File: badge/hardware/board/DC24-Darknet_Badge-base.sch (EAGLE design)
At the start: 54 parts, among them Q1 SOP22, SW0 SWITCH_TACTILETACTILE-2PIN-NA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, SW1 SWITCH_TACTILETACTILE-2PIN-NA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, SW2 SWITCH_TACTILETACTILE-2PIN-NA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, SW3 SWITCH_TACTILETACTILE-2PIN-NA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, SW4 SWITCH_TACTILETACTILE-2PIN-NA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, SW5 SWITCH_TACTILETACTILE-2PIN-NA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, SW6 SWITCH_TACTILETACTILE-2PIN-NA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, SW7 SWITCH_TACTILETACTILE-2PIN-NA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, SW8 SWITCH_TACTILETACTILE-2PIN-NA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

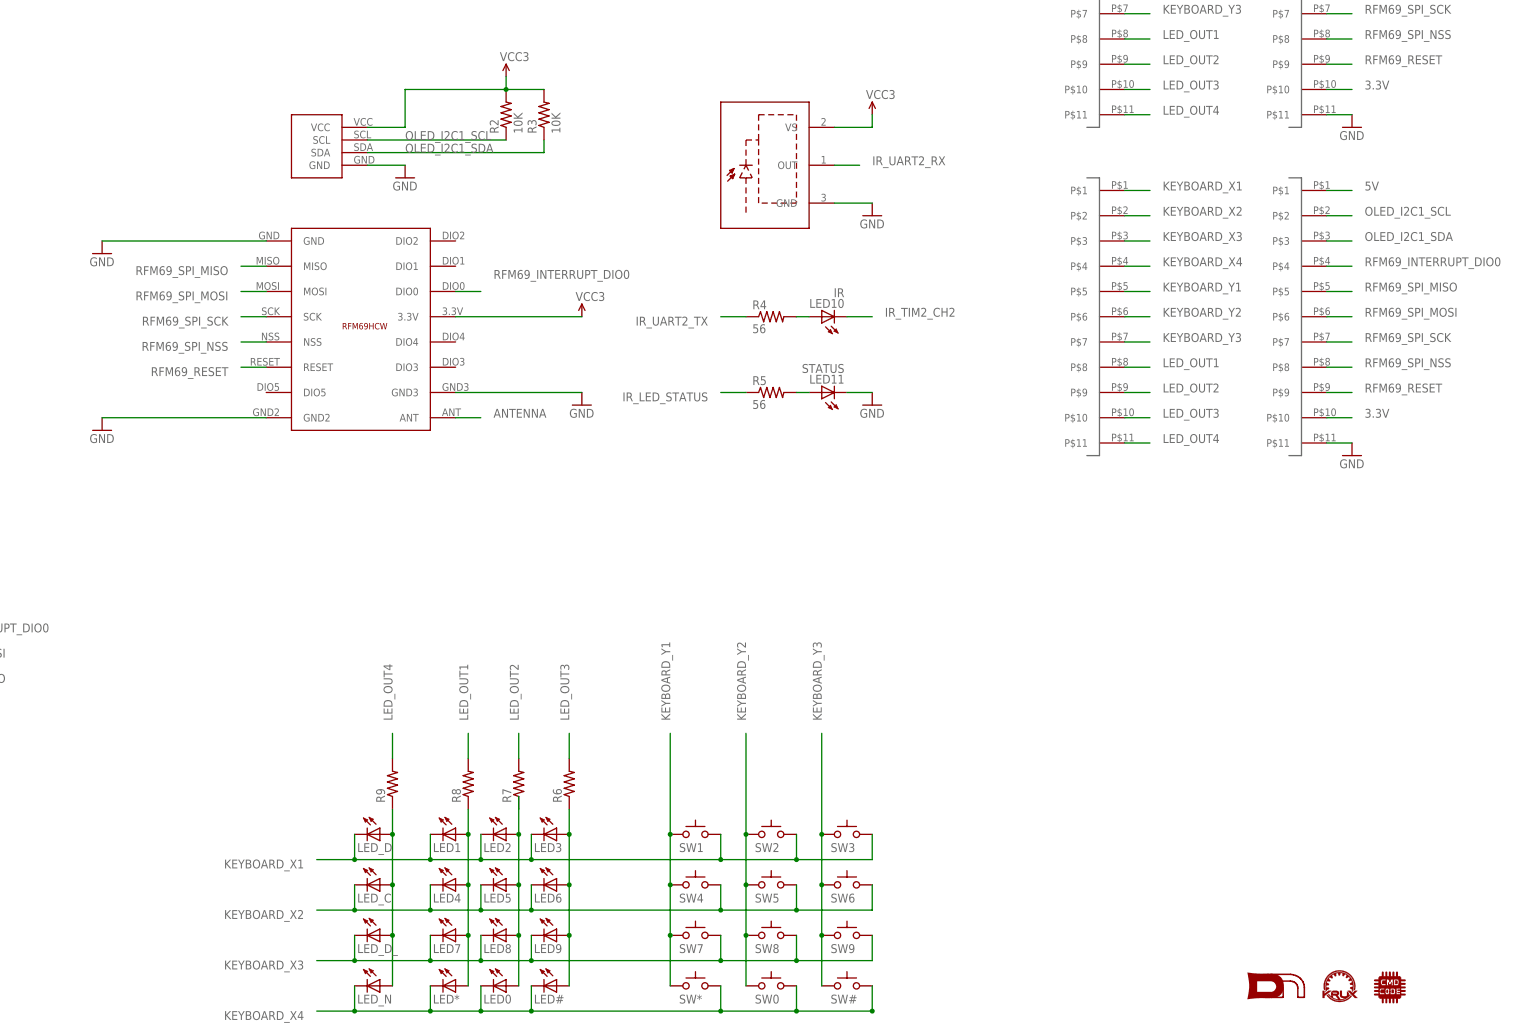
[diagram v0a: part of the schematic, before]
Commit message: moved board files over so we don't lose them
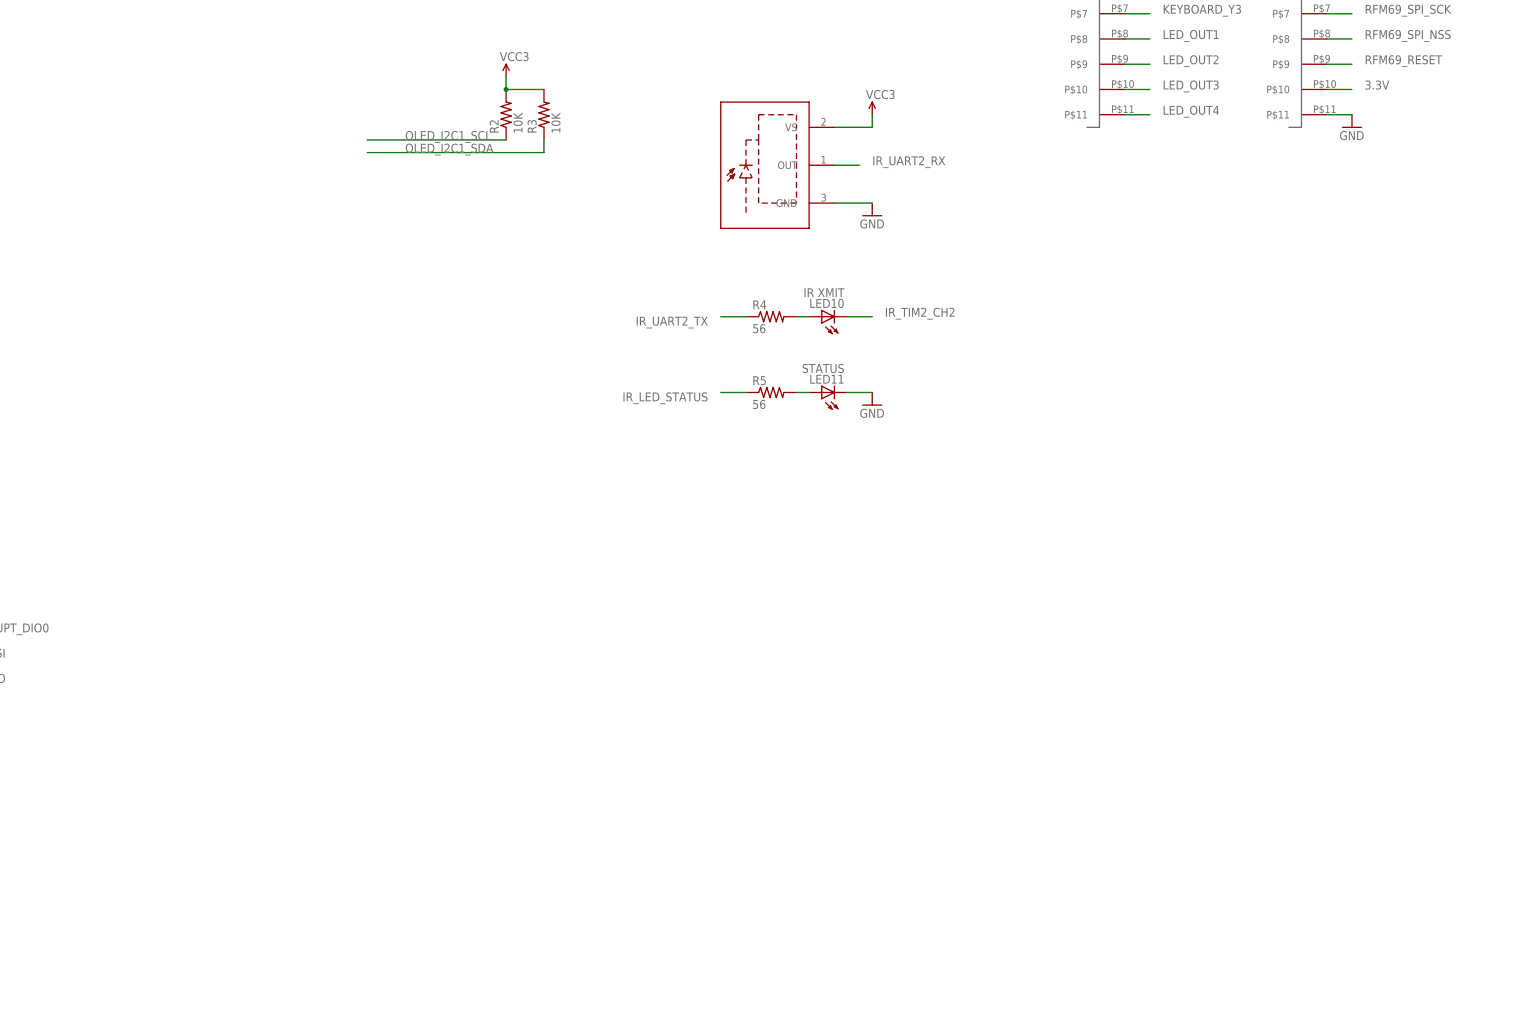
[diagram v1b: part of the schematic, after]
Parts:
- removed LED#, LED*, LED0, LED1, LED2, LED3, LED4, LED5, LED6, LED7, LED8, LED9, LED_C, LED_D, LED_D_, LED_N: (no value), SYNShop:LEDREVERSEMOUNT
- removed R6, R7, R8, R9: (no value), SYNShop:RESISTOR1206
- removed SW#, SW*, SW0, SW1, SW2, SW3, SW4, SW5, SW6, SW7, SW8, SW9: SWITCH_TACTILETACTILE-2PIN-NARROW, SYNShop:SWITCH_TACTILETACTILE-2PIN-NARROW
- removed U$1: I2C_0.96_OLEDOLED, SYNShop:I2C_0.96_OLEDOLED
- removed U$13, U$6: HEADER_11PIN, SYNShop:HEADER_11PIN
- removed U$2: RFM69HCWRFN69HCWSMD, SYNShop:RFM69HCWRFN69HCWSMD
- removed U$21: KRUX_LOGO, SYNShop:KRUX_LOGO
- removed U$22: DN_LOGO, SYNShop:DN_LOGO
- removed U$23: CMD_C0DE_LOGO, SYNShop:CMD_C0DE_LOGO
- LED10: value IR -> IR XMIT
- renumbered Q1 to U1
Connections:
- removed net ANTENNA: U$2.ANT
- removed net N$10: LED*.A, LED1.A, LED4.A, LED7.A, R8.1
- removed net N$11: LED_C.A, LED_D.A, LED_D_.A, LED_N.A, R9.1
- removed net N$8: LED#.A, LED3.A, LED6.A, LED9.A, R6.1
- removed net N$9: LED0.A, LED2.A, LED5.A, LED8.A, R7.1
- net 3.3V: no longer U$1.VCC, U$13.P$10, U$2.3.3V
- net 5V: no longer U$13.P$1
- net GND: no longer U$1.GND, U$13.P$11, U$2.GND, U$2.GND2, U$2.GND3
- net KEYBOARD_X1: no longer LED1.C, LED2.C, LED3.C, LED_D.C, SW1.A, SW2.A, SW3.A, U$6.P$1
- net KEYBOARD_X2: no longer LED4.C, LED5.C, LED6.C, LED_C.C, SW4.A, SW5.A, SW6.A, U$6.P$2
- net KEYBOARD_X3: no longer LED7.C, LED8.C, LED9.C, LED_D_.C, SW7.A, SW8.A, SW9.A, U$6.P$3
- net KEYBOARD_X4: no longer LED#.C, LED*.C, LED0.C, LED_N.C, SW#.A, SW*.A, SW0.A, U$6.P$4
- net KEYBOARD_Y1: no longer SW*.C, SW1.C, SW4.C, SW7.C, U$6.P$5
- net KEYBOARD_Y2: no longer SW0.C, SW2.C, SW5.C, SW8.C, U$6.P$6
- net KEYBOARD_Y3: no longer SW#.C, SW3.C, SW6.C, SW9.C, U$6.P$7
- net LED_OUT1: no longer R8.2, U$6.P$8
- net LED_OUT2: no longer R7.2, U$6.P$9
- net LED_OUT3: no longer R6.2, U$6.P$10
- net LED_OUT4: no longer R9.2, U$6.P$11
- net OLED_I2C1_SCL: no longer U$1.SCL, U$13.P$2
- net OLED_I2C1_SDA: no longer U$1.SDA, U$13.P$3
- net RFM69_INTERRUPT_DIO0: no longer U$13.P$4, U$2.DIO0
- net RFM69_RESET: no longer U$13.P$9, U$2.RESET
- net RFM69_SPI_MISO: no longer U$13.P$5, U$2.MISO
- net RFM69_SPI_MOSI: no longer U$13.P$6, U$2.MOSI
- net RFM69_SPI_NSS: no longer U$13.P$8, U$2.NSS
- net RFM69_SPI_SCK: no longer U$13.P$7, U$2.SCK
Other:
- note removed: "High"
- note removed: "Internal Pullup on inputs"
- note removed: "Low"
- note removed: "Only one LED lit at any time for each line, so only one resistor needed"
- note removed: "Pull High to enable line"
- note removed: "Pull Low to enable line"
